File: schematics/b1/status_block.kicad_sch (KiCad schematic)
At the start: 22 parts, among them Q1 2N3904, SW5 SW_SPDT, U4 74HC595

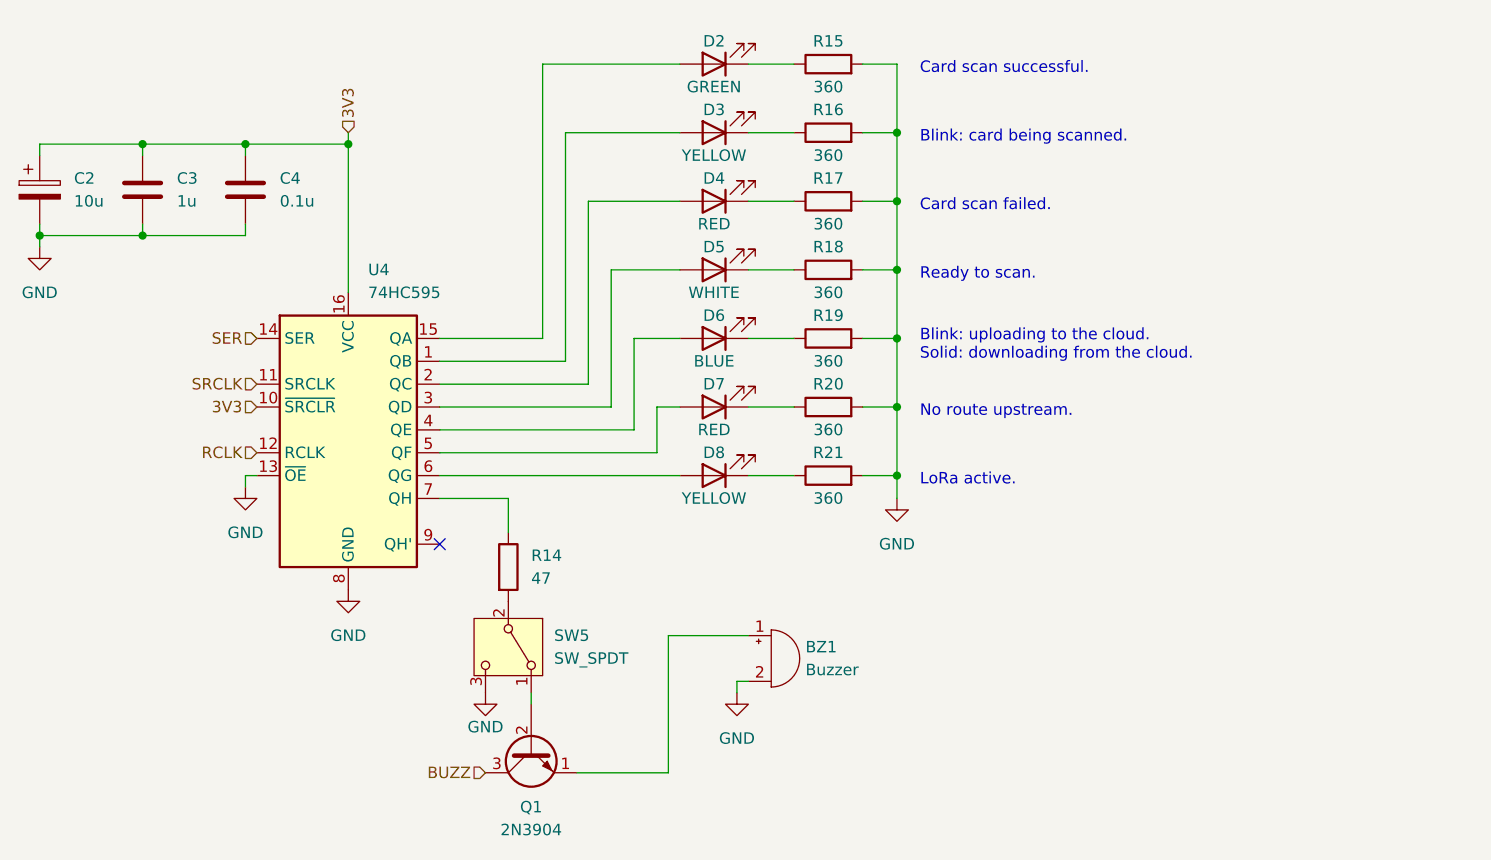
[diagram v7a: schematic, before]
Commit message: Wired LoRa and added a bulk to the status block.
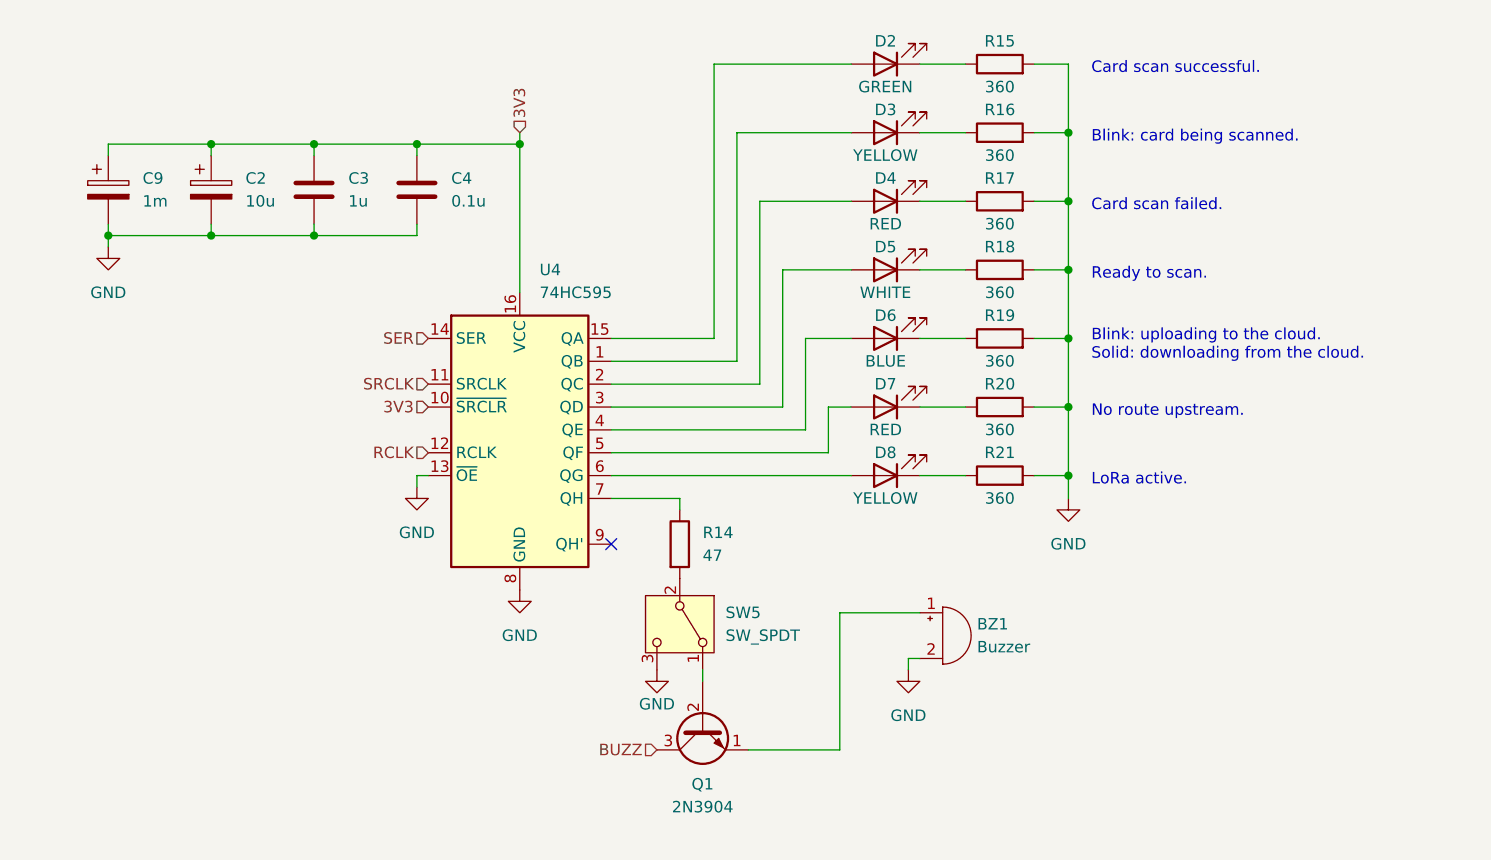
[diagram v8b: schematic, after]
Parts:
- added C9: 1m, symbol Device:C_Polarized
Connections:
- net 3V3: now also C9.1
- net GND: now also C9.2
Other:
- moved on the sheet: BZ1, C2, C3, C4, D2, D3, D4, D5, D6, D7, D8, Q1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
